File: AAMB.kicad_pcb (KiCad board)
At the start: 2 copper layers, 148.7 x 80.4 mm, 184 parts, among them J1 Screw_Terminal_01x04, J2 PJRAS4X2U01X, J3 SPKR, J4 SPKR, J5 Screw_Terminal_01x03, J6 Screw_Terminal_01x03, J7 Screw_Terminal_01x04, K1 G5LE-1, K2 G5LE-1, Q1 BC846, Q2 BC856, Q203 BC846, Q204 BCP53, Q205 BCP56, Q206 BCP53, Q207 MJL21193, Q208 MJL21194, Q209 BC846, Q3 BC846, Q303 BC846, Q304 BCP53, Q305 BCP56, Q306 BCP53, Q307 MJL21193, Q308 MJL21194, Q309 BC846, Q4 BCP53, U1 TL072, U2 NE5532, U201 BC846BDW1T1G, U3 NE5532, U301 BC846BDW1T1G, U4 THAT2180, U5 DG509BEQ-T1-E3, U6 CD4071B

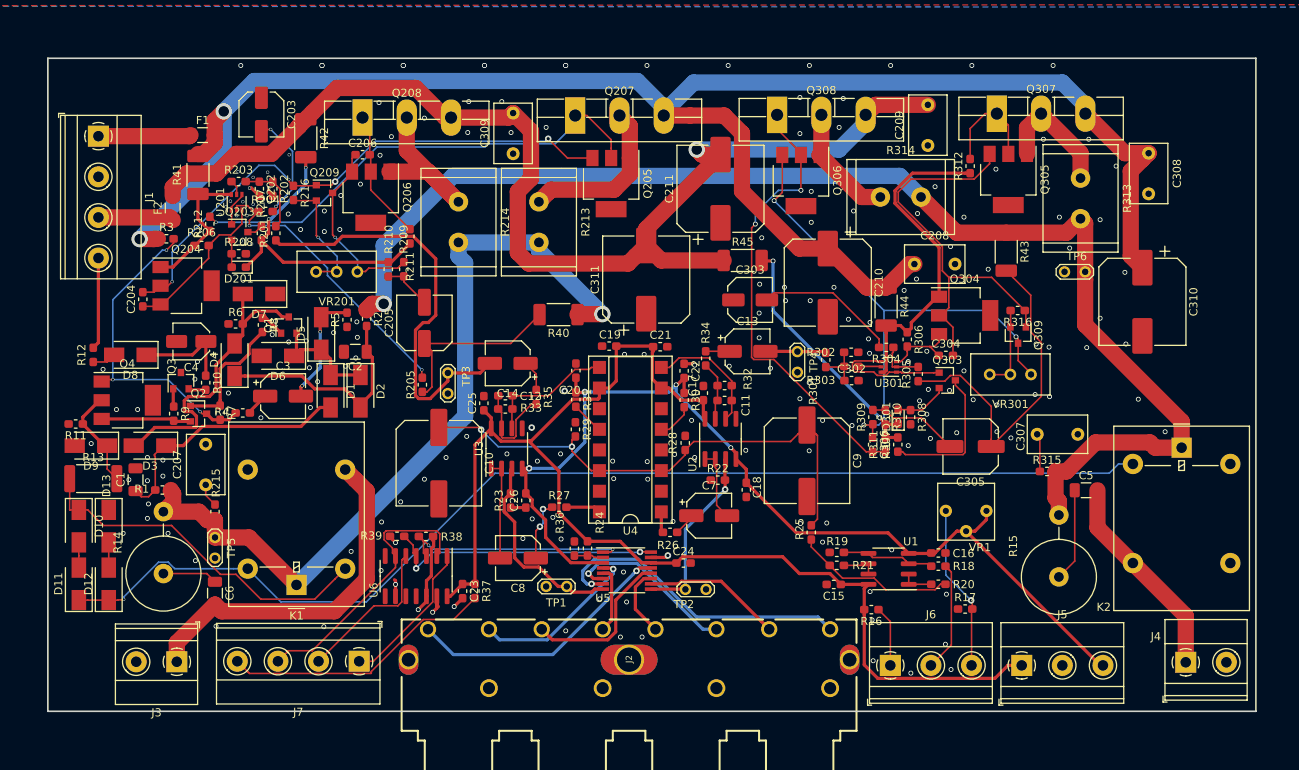
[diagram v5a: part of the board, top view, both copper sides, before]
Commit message: Layout complete. Screw holes added and connected to GND.
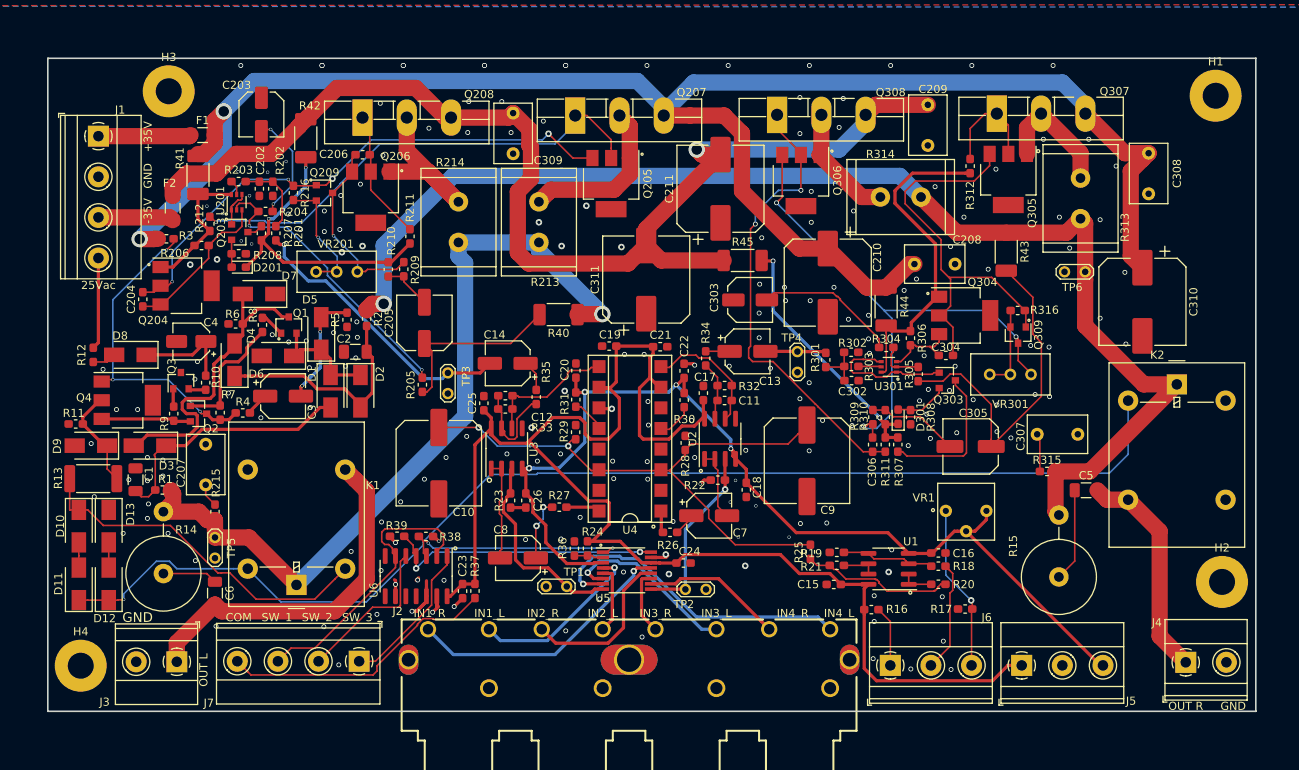
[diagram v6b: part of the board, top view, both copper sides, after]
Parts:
- added H1: MountingHole_Pad, MountingHole:MountingHole_3.2mm_M3_Pad, F.Cu at (211.6, 50.7)
- added H2: MountingHole_Pad, MountingHole:MountingHole_3.2mm_M3_Pad, F.Cu at (212.4, 110.6)
- added H3: MountingHole_Pad, MountingHole:MountingHole_3.2mm_M3_Pad, F.Cu at (82.7, 50.2)
- added H4: MountingHole_Pad, MountingHole:MountingHole_3.2mm_M3_Pad, F.Cu at (71.9, 120.9)
- moved K2 7.82 mm to (206.8, 86.2)
- moved R25 2.39 mm to (161.7, 106.9)
- moved R306 0.42 mm to (174.0, 80.6)
- moved R29 0.34 mm to (132.8, 92.1)
- moved U4 0.12 mm to (139.5, 92.9)
- moved U2 0.05 mm to (150.6, 92.9)
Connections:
- net /input_select/IN1_L renamed /IN1_L
- net /input_select/IN1_R renamed /IN1_R
- net /input_select/IN2_L renamed /IN2_L
- net /input_select/IN2_R renamed /IN2_R
- net /input_select/IN3_L renamed /IN3_L
- net /input_select/IN3_R renamed /IN3_R
- net /input_select/IN4_L renamed /IN4_L
- net /input_select/IN4_R renamed /IN4_R
- net /input_select/input_sw_1 renamed /input_sw_1
- net /input_select/input_sw_2 renamed /input_sw_2
- net /input_select/input_sw_3 renamed /input_sw_3
- net /input_select/input_sw_com renamed /input_sw_com
- net /short_protection_muting/audio_rly_out_L renamed /audio_rly_out_L
- net /short_protection_muting/audio_rly_out_R renamed /audio_rly_out_R
- net /volume/vol_pot_1 renamed /vol_pot_1
- net /volume/vol_pot_2 renamed /vol_pot_2
- net /volume/vol_pot_3 renamed /vol_pot_3
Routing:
- net +12V: track 154.0 -> 179.3 mm
- net /line_audio_L: track 51.4 -> 35.1 mm, vias 0 -> 1
- net /volume/v_ec-: track 65.1 -> 73.6 mm
- net /short_protection_muting/RLY_-L_+R: track 140.9 -> 148.0 mm
- net /pwr_audio_R: track 158.8 -> 155.3 mm
- net GND: track 26.2 -> 23.9 mm, vias 191 -> 199
- net /audio_rly_out_R: track 25.7 -> 27.2 mm
- net /input_sw_3: track 34.1 -> 35.6 mm
- net Net-(D3-Pad2): track 37.3 -> 38.4 mm
- net /IN4_L: track 38.4 -> 39.6 mm
- net Net-(R20-Pad1): track 19.9 -> 18.8 mm
- net Net-(C306-Pad1): track 67.2 -> 68.3 mm
- net Net-(C204-Pad2): track 68.5 -> 67.5 mm
- net Net-(Q303-Pad1): track 15.7 -> 16.6 mm
- net Net-(C304-Pad2): track 51.0 -> 50.1 mm
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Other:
- net class Default: clearance 0.1 -> 0.2
- net class VCC_audio: clearance 0.1 -> 0.2
- rule trace_clearance: 0.1 -> 0.2
- board text added: "+35V"
- board text added: "-35V"
- board text added: "25Vac"
- board text added: "COM"
- board text added: "GND"
- board text added: "IN1_L"
- board text added: "IN1_R"
- board text added: "IN2_L"
- board text added: "IN2_R"
- board text added: "IN3_L"
- board text added: "IN3_R"
- board text added: "IN4_L"
- board text added: "IN4_R"
- board text added: "OUT L"
- board text added: "OUT R"
- board text added: "SW_1"
- board text added: "SW_2"
- board text added: "SW_3"

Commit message: Updating files with Rev02
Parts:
- removed VR1: 5k, Potentiometer_THT:Nidec_CT6EP202
- added J10: RCJ-2221, Library_AAMB-Rev02:RCJ-2221, F.Cu at (-42.4, -163.6)
- added J8: RCJ-2221, Library_AAMB-Rev02:RCJ-2221, F.Cu at (-82.4, -163.6)
- added J9: RCJ-2221, Library_AAMB-Rev02:RCJ-2221, F.Cu at (-62.4, -163.6)
- added R46: 3203X502P_TEC, Library_AAMB-Rev02:3203X502P, F.Cu at (-138.0, -187.4)
- C1, C2: moved to B.Cu
- C11, C12, C202, C204, C206, C23, C302, C304, C306: footprint Capacitor_SMD:C_0603_1608Metric_Pad1.05x0.95mm_HandSolder -> Capacitor_SMD:C_0603_1608Metric_Pad1.08x0.95mm_HandSolder
- C15, C16, C17, C18, C19, C20, C21, C22, C24, C25, C26: footprint Capacitor_SMD:C_0603_1608Metric_Pad1.05x0.95mm_HandSolder -> Capacitor_SMD:C_0603_1608Metric_Pad1.08x0.95mm_HandSolder; moved to B.Cu
- D1, D10, D12, D2, D3, D4, D5, D6, D7, D8, D9: footprint Diode_SMD:D_SMA -> Diode_THT:D_DO-41_SOD81_P10.16mm_Horizontal
- F1, F2: footprint Resistor_SMD:R_1206_3216Metric_Pad1.42x1.75mm_HandSolder -> Resistor_SMD:R_1206_3216Metric_Pad1.30x1.75mm_HandSolder
- J2: value PJRAS4X2U01X -> RCJ-2221; footprint Connectors-amp:PJRAS4X2U01X -> Library_AAMB-Rev02:RCJ-2221
- Q1, Q3: footprint Package_TO_SOT_SMD:SOT-23 -> Package_TO_SOT_THT:TO-92_Inline
- Q4: footprint Package_TO_SOT_SMD:SOT-223 -> Package_TO_SOT_THT:TO-126-3_Vertical
- R1, R10, R11, R12, R16, R17, R18, R19, R2, R20, R201, R202, R203, R204, R205, R206, R207, R208, R209, R21, R210, R211, R212, R215, R216, R25, R26, R27, R3, R301, R302, R303, R304, R305, R306, R307, R308, R309, R310, R311, R312, R315, R316, R32, R33, R34, R35, R4, R5, R7, R8, R9: footprint Resistor_SMD:R_0603_1608Metric_Pad1.05x0.95mm_HandSolder -> Resistor_SMD:R_0201_0603Metric_Pad0.64x0.40mm_HandSolder
- R22, R23, R24, R28, R29, R30, R31, R36, R37, R38, R39, R6: footprint Resistor_SMD:R_0603_1608Metric_Pad1.05x0.95mm_HandSolder -> Resistor_SMD:R_0201_0603Metric_Pad0.64x0.40mm_HandSolder; moved to B.Cu
- R40, R41, R42, R43, R44, R45: footprint Resistor_SMD:R_2010_5025Metric_Pad1.52x2.65mm_HandSolder -> Resistor_SMD:R_2010_5025Metric
- TP1, TP2, TP3, TP4, TP5, TP6: value TP -> TestPoint; footprint TestPoint:TestPoint_2Pads_Pitch2.54mm_Drill0.8mm -> TestPoint:TestPoint_Keystone_5000-5004_Miniature
- moved J5 472.0 mm to (-146.5, -212.5), turned to -90 degrees
- moved J6 448.4 mm to (-146.5, -195.2), turned to -90 degrees
- moved R17 437.8 mm to (-139.2, -184.8), turned to 180 degrees
- moved R16 436.9 mm to (-139.3, -195.4), turned to 0 degrees
- moved C9 399.6 mm to (-78.8, -223.8), turned to 90 degrees
- moved R20 395.1 mm to (-75.3, -192.9), turned to -90 degrees
- moved R18 391.4 mm to (-78.6, -187.4), turned to 180 degrees
- moved J7 390.9 mm to (-146.5, -177.9), turned to -90 degrees
- moved R26 390.5 mm to (-80.9, -214.4), turned to 0 degrees
- moved TP4 389.4 mm to (-89.0, -217.1), turned to 0 degrees
- moved C7 388.6 mm to (-82.5, -209.5), turned to -90 degrees
- moved C16 387.7 mm to (-76.9, -185.6), turned to 0 degrees
- moved U1 385.8 mm to (-73.5, -189.2), turned to 0 degrees
- moved R21 384.8 mm to (-74.3, -192.9), turned to -90 degrees
- moved C18 384.5 mm to (-85.9, -201.4), turned to 0 degrees
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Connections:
- net /audio_rly_out_L renamed /short_protection_muting/audio_rly_out_L
- net /audio_rly_out_R renamed /short_protection_muting/audio_rly_out_R
- net /input_sw_1 renamed /source_select/input_sw_1
- net /input_sw_2 renamed /source_select/input_sw_2
- net /input_sw_3 renamed /source_select/input_sw_3
- net /input_sw_com renamed /source_select/input_sw_com
- net /vol_pot_1 renamed /volume/vol_pot_1
- net /vol_pot_2 renamed /volume/vol_pot_2
- net /vol_pot_3 renamed /volume/vol_pot_3
- J2 pad 1: (no net) -> GND
- J2 pad 2: (no net) -> /IN1_R
- J2 pad 3: (no net) -> /IN1_L
- U4 pad 13: Net-(U4-Pad13) -> unconnected-(U4-Pad13)
- U4 pad 4: Net-(U4-Pad4) -> unconnected-(U4-Pad4)
- U6 pad 10: Net-(U6-Pad10) -> unconnected-(U6-Pad10)
- U6 pad 11: Net-(U6-Pad11) -> unconnected-(U6-Pad11)
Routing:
- net +35V: track 213.7 -> 0.00 mm, vias 2 -> 0
- net +12V: track 179.3 -> 0.00 mm
- net /pwr_audio_R: track 155.3 -> 0.00 mm, vias 1 -> 0
- net /short_protection_muting/RLY_-L_+R: track 148.0 -> 0.00 mm, vias 1 -> 0
- net -35V: track 145.6 -> 0.00 mm, vias 1 -> 0
- net -12V: track 126.7 -> 0.00 mm, vias 4 -> 0
- net /pwr_audio_L: track 100.8 -> 0.00 mm, vias 1 -> 0
- net /volume/v_ec-: track 73.6 -> 0.00 mm, vias 2 -> 0
- net Net-(C306-Pad1): track 68.3 -> 0.00 mm, vias 3 -> 0
- net Net-(C204-Pad2): track 67.5 -> 0.00 mm, vias 4 -> 0
- net Net-(Q205-Pad2): track 59.5 -> 0.00 mm, vias 1 -> 0
- net Net-(C306-Pad2): track 57.0 -> 0.00 mm, vias 2 -> 0
- net Net-(C304-Pad2): track 50.1 -> 0.00 mm
- net /short_protection_muting/audio_rly_out_L: track 44.2 -> 0.00 mm
- net /short_protection_muting/RLY_+L: track 43.9 -> 0.00 mm
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- removed copper zone on B.Cu, net GND
- removed copper zone on F.Cu, net GND
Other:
- board size 148.7 x 80.4 mm -> 16.2 x 3 mm
- copper layers 2 -> 6
- net class Default removed
- net class N35V removed
- net class P35V removed
- net class VCC_audio removed
- net class audio_pwr_neg removed
- net class audio_pwr_pos removed
- board text added: "Audio Amp L"
- board text added: "Audio Amp R"
- board text added: "Source Select"
- board text removed: "+35V"
- board text removed: "-35V"
- board text removed: "25Vac"
- board text removed: "COM"
- board text removed: "GND"
- board text removed: "IN1_L"
- board text removed: "IN1_R"
- board text removed: "IN2_L"
- board text removed: "IN2_R"
- board text removed: "IN3_L"
- board text removed: "IN3_R"
- board text removed: "IN4_L"
- board text removed: "IN4_R"
- board text removed: "OUT L"
- board text removed: "OUT R"
- board text removed: "SW_1"
- board text removed: "SW_2"
- board text removed: "SW_3"

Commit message: Minor layout updates.
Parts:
- R306: moved to B.Cu
- moved H4 161.5 mm to (-134.6, -246.4)
- moved H3 137.4 mm to (-7.62, -246.4)
- moved H1 128.8 mm to (-134.6, -152.4)
- moved C210 89.4 mm to (77.8, -185.4), turned to -90 degrees
- moved Q307 89.3 mm to (145.8, -137.0)
- moved C308 88.6 mm to (99.2, -126.1), turned to -90 degrees
- moved C310 85.7 mm to (89.4, -121.8), turned to -90 degrees
- moved D301 75.7 mm to (81.4, -101.8)
- moved R45 65.4 mm to (211.4, -112.4), turned to 180 degrees
- moved Q309 60.3 mm to (66.9, -91.2), turned to 180 degrees
- moved R310 57.9 mm to (77.6, -106.0)
- moved R309 54.9 mm to (63.6, -104.4), turned to 90 degrees
- moved Q304 53.1 mm to (75.4, -88.0), turned to -90 degrees
- moved H2 51.3 mm to (-7.62, -152.4)
- moved C306 50.8 mm to (63.6, -101.6), turned to 180 degrees
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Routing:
- net Net-(C306-Pad1): track 0.00 -> 20.3 mm
- net Net-(C304-Pad2): track 0.00 -> 11.6 mm
- net /audio_pwr_R/P35_low_pow_R: track 0.00 -> 10.8 mm, vias 0 -> 2
- net Net-(C305-Pad2): track 0.00 -> 10.7 mm
- net Net-(Q309-Pad2): track 0.00 -> 10.6 mm
- net Net-(C304-Pad1): track 0.00 -> 7.55 mm
- net Net-(D301-Pad2): track 0.00 -> 7.24 mm
- net /line_audio_R: track 0.00 -> 6.49 mm
- net /audio_pwr_R/N35_low_pow_R: track 0.00 -> 6.41 mm
- net Net-(Q303-Pad1): track 0.00 -> 6.40 mm
- net Net-(C305-Pad1): track 0.00 -> 5.78 mm
- net Net-(C302-Pad1): track 0.00 -> 5.58 mm
- net Net-(C303-Pad2): track 0.00 -> 3.67 mm
- net Net-(Q303-Pad3): track 0.00 -> 2.58 mm
- net Net-(R304-Pad1): track 0.00 -> 2.40 mm
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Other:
- board text removed: "Source Select"
